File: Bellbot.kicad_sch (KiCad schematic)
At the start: 2 parts, among them U1 NUCLEO144-F767ZI

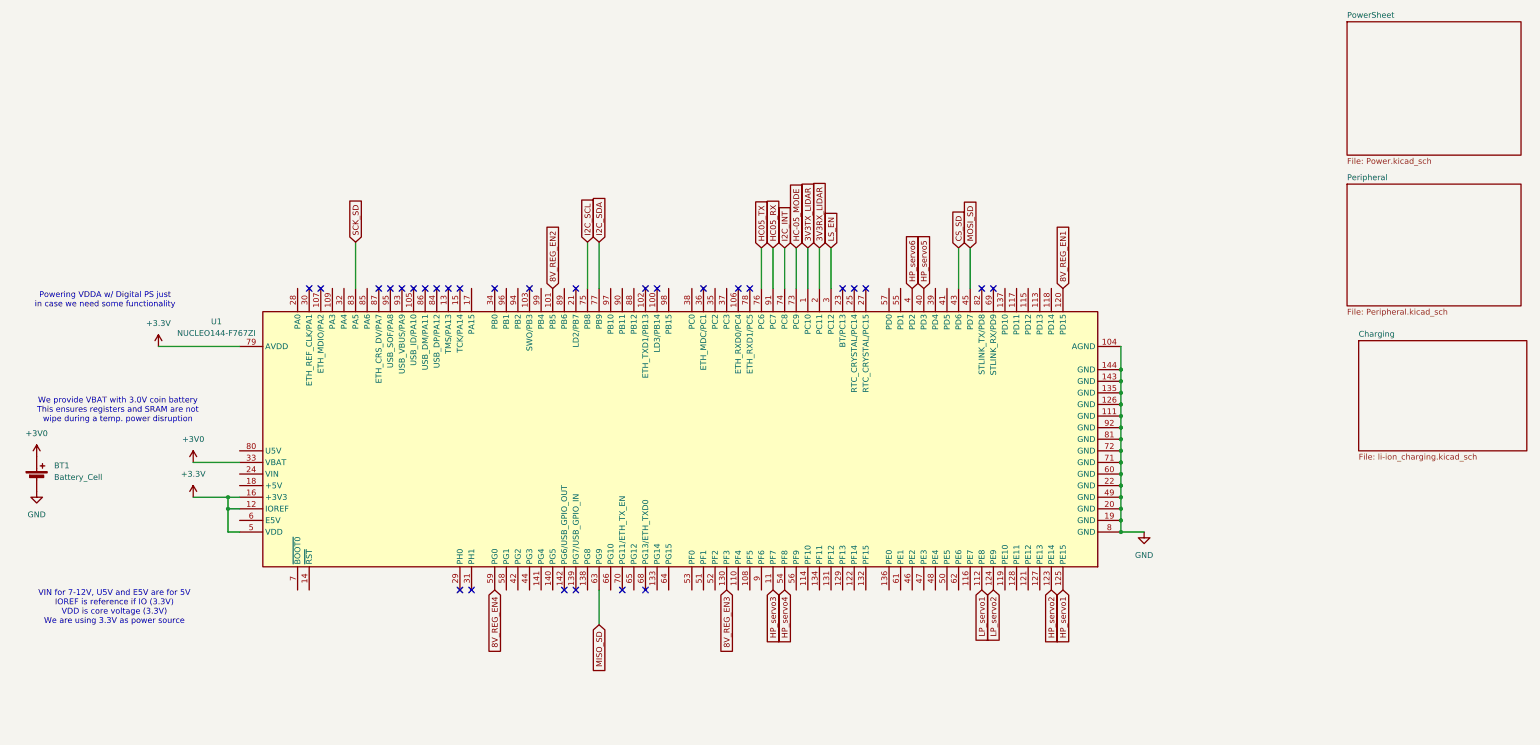
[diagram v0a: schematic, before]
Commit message: General Layout Complete
Completed general layout, beginning to add debugging components such as test points and
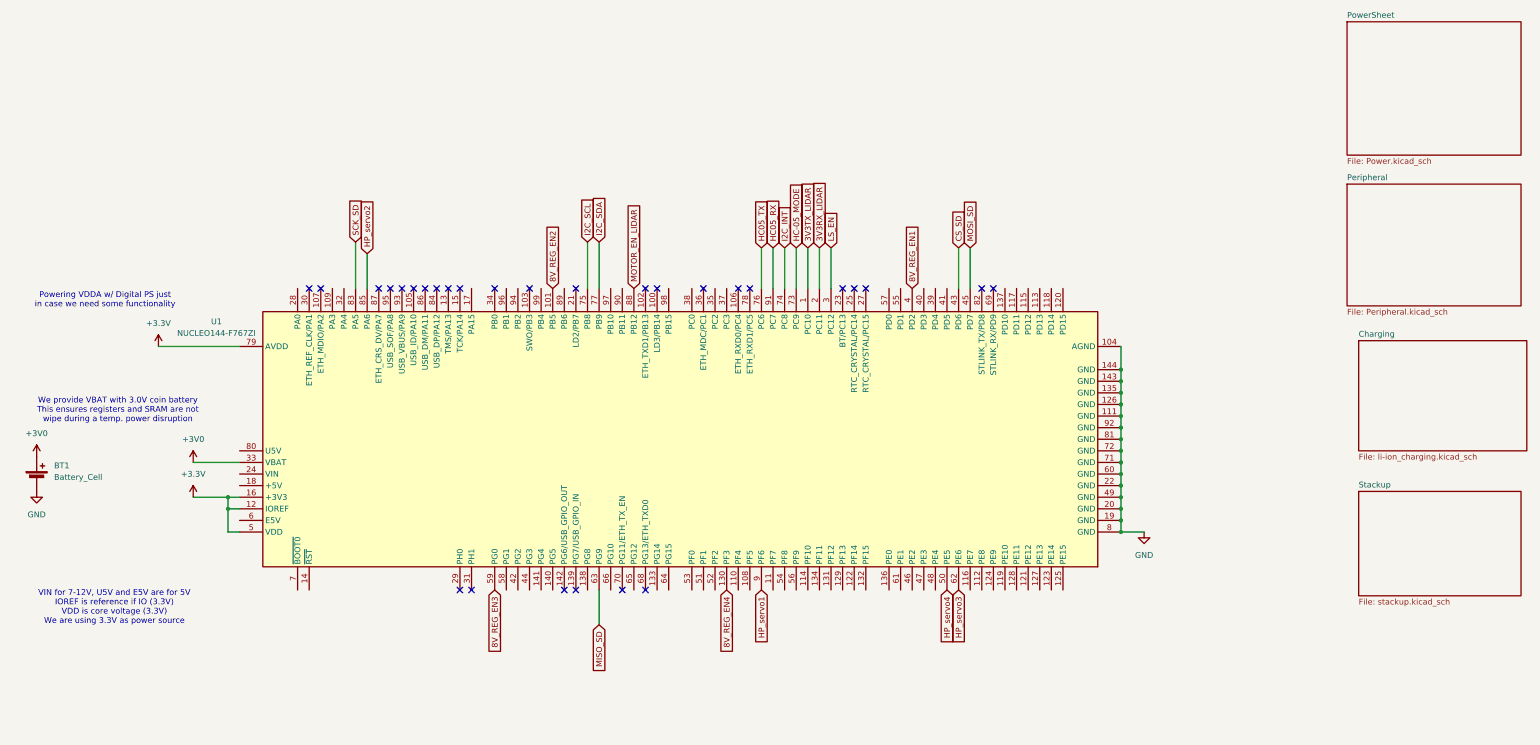
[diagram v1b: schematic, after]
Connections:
- net HP_servo6 is gone; now on net 8V_REG_EN1: U1.4 (PD2)
- net 8V_REG_EN1: no longer U1.120 (PD15)
- net 8V_REG_EN3: now also U1.59 (PG0); no longer U1.130 (PF3)
- net 8V_REG_EN4: now also U1.130 (PF3); no longer U1.59 (PG0)
- net HP_servo1: now also U1.9 (PF6); no longer U1.125 (PE15)
- net HP_servo2: now also U1.85 (PA6); no longer U1.123 (PE14)
- net HP_servo3: now also U1.62 (PE6); no longer U1.11 (PF7)
- net HP_servo4: now also U1.50 (PE5); no longer U1.54 (PF8)
- net MOTOR_EN_LIDAR: now reaches U1.88 (PB12)
- net HP_servo5: no longer names the net of U1.40 (PD3)
- net LP_servo1: no longer names the net of U1.112 (PE8)
- net LP_servo2: no longer names the net of U1.124 (PE9)
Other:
- added sheet Stackup (stackup.kicad_sch)

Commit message: testpoints on board
Organized testpoints on board. Still need to fix bus for general purpose GPIO and route traces for LEDs.
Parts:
- added D10: LED, Capacitor_SMD:C_0603_1608Metric_Pad1.08x0.95mm_HandSolder, symbol Device:LED
- added R22: 65, Resistor_SMD:R_0805_2012Metric_Pad1.20x1.40mm_HandSolder, symbol Device:R_Small_US
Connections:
- net GND: now also D10.1 (K)
- net GPIO_Gen1: now reaches U1.112 (PE8)
- net QUADSPI_IO3: now reaches U1.113 (PD13)
- net QUADSPI_CLK: now reaches U1.114 (PF10)
- net GPIO_Gen0: now reaches U1.116 (PE7)
- net GPIO_Gen3: now reaches U1.119 (PE10)
- net GPIO_Gen5: now reaches U1.121 (PE12)
- net I2C_Extra_SCL: now reaches U1.122 (PF14)
- net GPIO_Gen7: now reaches U1.123 (PE14)
- net GPIO_Gen2: now reaches U1.124 (PE9)
- net GPIO_Gen8: now reaches U1.125 (PE15)
- net GPIO_Gen6: now reaches U1.127 (PE13)
- net GPIO_Gen4: now reaches U1.128 (PE11)
- net I2C_Extra_SDA: now reaches U1.132 (PF15)
- net at U1.44 (PG3): now also R22.1
- net QUADSPI_IO2: now reaches U1.46 (PE2)
- net QUADSPI_IO0: now reaches U1.54 (PF8)
- net QUADSPI_IO1: now reaches U1.56 (PF9)
- net QUADSPI_NCS: now reaches U1.97 (PB10)
- new net: D10.2 (A), R22.2
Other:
- added sheet Extra Breakout Pins (Extra.kicad_sch)
